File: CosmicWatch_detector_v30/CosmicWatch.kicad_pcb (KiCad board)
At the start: 2 copper layers, 140.8 x 104 mm, 115 parts, among them J3 RJ45, P1 CONN_01X04, P10 CONN_02X02, P11 CONN_01X01, P12 CONN_01X01, P13 CONN_01X01, P14 CONN_01X01, P15 CONN_02X04, P16 CONN_01X02, P19 CONN_01X01, P2 CONN_01X01, P29 CONN_01X01, P3 CONN_01X04, P30 CONN_01X01, P32 CONN_01X04, P4 CONN_01X04, P5 CONN_01X02, P7 CONN_01X01, P8 CONN_01X01, SW1 RESET, U1 MAX5026, U10 SiPM_AFBR-S4N33C013, U12 LTC6752, U13 TS5A1066, U16 UMCC, U17 UMCC, U19 LMH6658, U2 SiPM_MicroFJ−300XX−TSV, U22 UMCC, U23 UMCC, U3 MMCX, U4 TS5A1066, U5 RasberryPi_Pico, U6 LMH6658, U7 TPS6040X, U8 sd_card_socket, U9 2NPNMBT6429DW1T1G

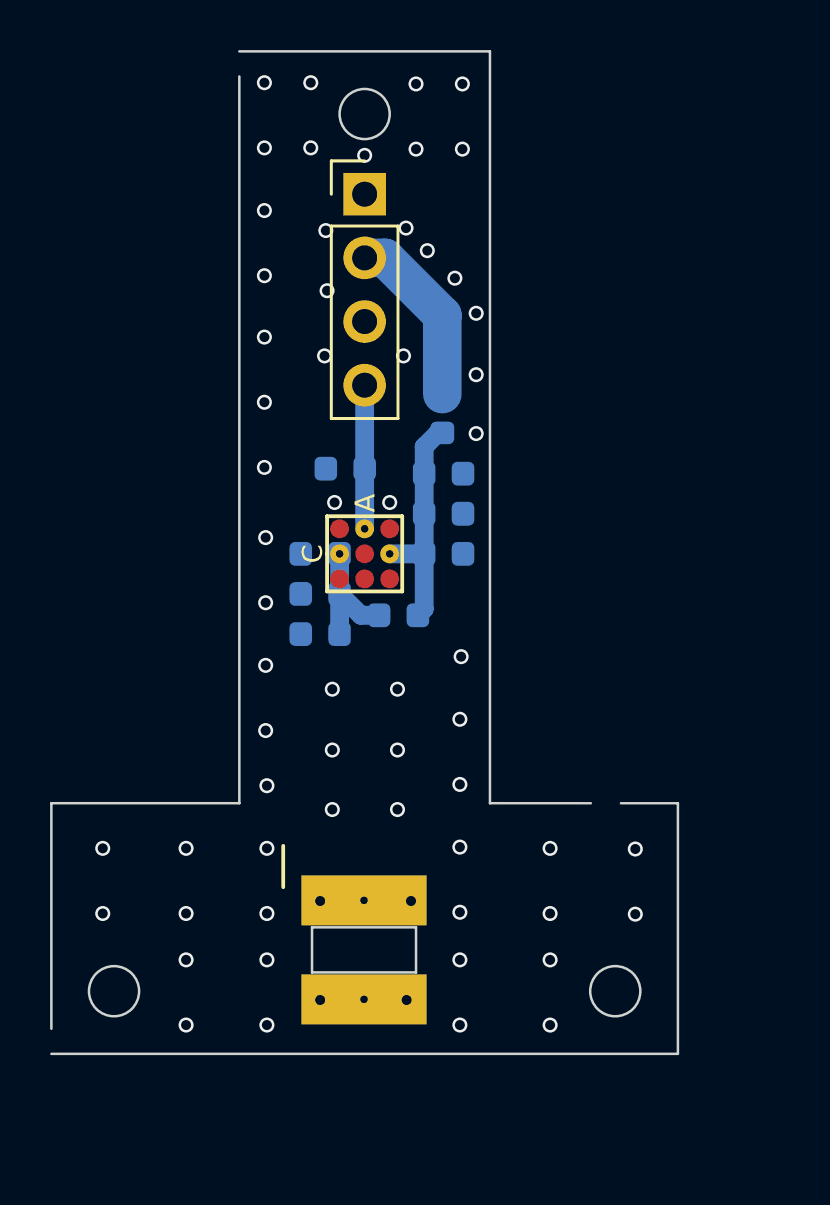
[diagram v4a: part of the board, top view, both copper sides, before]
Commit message: removing second sipm
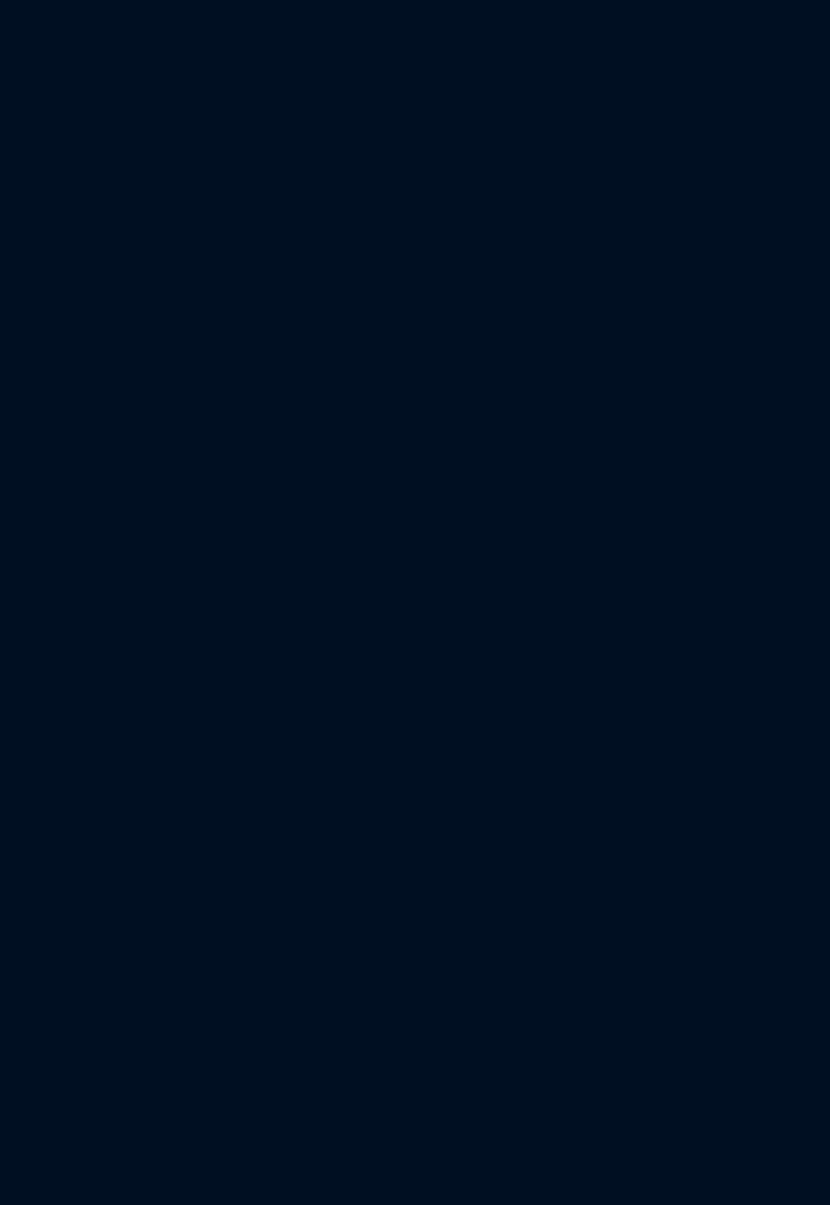
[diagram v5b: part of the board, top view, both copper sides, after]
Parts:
- removed C29, C34: 100n, Capacitor_SMD:C_0603_1608Metric
- removed C30, C33: 10nF, Capacitor_SMD:C_0603_1608Metric
- removed C31, C32: 10p, Capacitor_SMD:C_0603_1608Metric
- removed P29, P30: CONN_01X01, Connector_PinHeader_2.54mm:PinHeader_1x01_P2.54mm_Vertical
- removed P32: CONN_01X04, Connector_PinHeader_2.54mm:PinHeader_1x04_P2.54mm_Vertical
- removed R22, R34, R35: 10, Capacitor_SMD:C_0603_1608Metric
- removed U10: SiPM_AFBR-S4N33C013, MyFootprints:SiPM_S4N33C013
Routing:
- net Net-(U10-c2): track 9.16 -> 0.00 mm
- net Net-(P32-P2): track 7.19 -> 0.00 mm
- net Net-(P32-P4): track 5.73 -> 0.00 mm
- net Net-(U10-c1): track 5.13 -> 0.00 mm
- net unconnected-(P30-P1-Pad1): vias 2 -> 0
- net unconnected-(P29-P1-Pad1): vias 2 -> 0
- net GNDA: vias 298 -> 238
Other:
- board size 140.8 x 104 mm -> 99.9 x 99.9 mm
- board text removed: "AFBR-S4N33C013"

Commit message: updating netlist and deleting unnecessary components from PCB
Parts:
- removed C21, C35, C45: 0.1uF, Capacitor_SMD:C_0603_1608Metric
- removed C23, C43, C44, C5: 10nF, Capacitor_SMD:C_0603_1608Metric
- removed C36, C46: 2nF, Capacitor_SMD:C_0603_1608Metric
- removed C38: 2.2uF, Capacitor_SMD:C_0603_1608Metric
- removed C48: 1nF, Capacitor_SMD:C_0603_1608Metric
- removed R15, R16: 200, Capacitor_SMD:C_0603_1608Metric
- removed R18, R24, R40, R42: 100k, Capacitor_SMD:C_0603_1608Metric
- removed R19, R21, R31: 10k, Capacitor_SMD:C_0603_1608Metric
- removed R23: 20, Capacitor_SMD:C_0603_1608Metric
- removed R28: 100, Capacitor_SMD:C_0603_1608Metric
- removed R5: 1k, Capacitor_SMD:C_0603_1608Metric
- removed U12: LTC6752, Package_TO_SOT_SMD:SOT-23-6
- removed U19: LMH6658, Package_SO:SOIC-8_3.9x4.9mm_P1.27mm
- removed U22, U23: UMCC, MyFootprints:UMCC
- removed U4: TS5A1066, Package_TO_SOT_SMD:SOT-23-5
- added C10: 10n, Capacitor_SMD:C_0603_1608Metric, F.Cu at (118.2, 82.4)
- added C11: 2nF, Capacitor_SMD:C_0603_1608Metric, F.Cu at (118.2, 84.9)
- added C12: 0.1uF, Capacitor_SMD:C_0603_1608Metric, F.Cu at (118.2, 87.4)
- added C13: 10nF, Capacitor_SMD:C_0603_1608Metric, F.Cu at (118.2, 89.9)
- added C18: 10nF, Capacitor_SMD:C_0603_1608Metric, F.Cu at (118.2, 92.4)
- added C9: 10nF, Capacitor_SMD:C_0603_1608Metric, F.Cu at (118.2, 79.9)
- added Q1: 2N7002, Package_TO_SOT_SMD:SOT-23, F.Cu at (122.7, 80.8)
- C19: value 0.1uF -> 10n
- C6: value 10nF -> 0.1uF
- C8: value 10n -> 10nF
- D2, D3: value DIODE -> D_Schottky; footprint Diode_SMD:D_SOD-123 -> Diode_SMD:D_SOD-523
- R1: value 200 -> 47k
- R11: value 47k -> 100
- R13: value 150 -> 10k
- R14: value 2k -> 100
- R4: value 200 -> 1k
- R6: value 49.9 -> 10k
- R9: value 1k -> 100
- U9: value 2NPNMBT6429DW1T1G -> LMH6658; footprint Package_TO_SOT_SMD:SOT-23-6 -> Package_SO:SOIC-8_3.9x4.9mm_P1.27mm
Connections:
- C19 pad 1: GNDA -> VCC
- C19 pad 2: VEE -> GNDA
- C6 pad 1: VCC -> GNDA
- C6 pad 2: GNDA -> VEE
- C8 pad 1: VCC -> GNDA
- C8 pad 2: GNDA -> VEE
- D2 pad 1: Net-(D2-A) -> Net-(D2-K)
- D2 pad 2: Net-(D2-K) -> Net-(D2-A)
- D3 pad 1: SNG2 -> Net-(D3-K)
- D3 pad 2: Net-(D2-A) -> Net-(D2-K)
- R1 pad 1: Net-(C46-Pad1) -> SiPM
- R1 pad 2: SNG2 -> GNDA
- R11 pad 1: SiPM -> SNG1
- R11 pad 2: GNDA -> Net-(D2-K)
- R12 pad 1: AMP1 -> GNDA
- R12 pad 2: Net-(U19--INA) -> Net-(Q1-D)
- R13 pad 1: Net-(U6--INA) -> VCC
- R13 pad 2: GNDA -> Net-(U9--INB)
- R14 pad 1: AMP2 -> GNDA
- R14 pad 2: Net-(U6--INA) -> Net-(U9--INB)
- R3 pad 2: Net-(U19-+INA) -> Net-(U6-+INA)
- R4 pad 1: Net-(D2-A) -> Net-(U6--INA)
- R4 pad 2: Net-(U6-OUTB) -> GNDA
- R6 pad 2: Net-(U6-+INA) -> Net-(U6--INA)
- R9 pad 1: Net-(U19--INA) -> Net-(Q1-D)
- R9 pad 2: GNDA -> Net-(D3-K)
- U5 pad 31: SNG2 -> unconnected-(U5-ADC0-Pad31)
- U6 pad 1: AMP2 -> AMP1
- U6 pad 5: AMP2 -> AMP1
- U6 pad 6: Net-(D2-K) -> Net-(Q1-D)
- U6 pad 7: Net-(U6-OUTB) -> Net-(D2-A)
- U9 pad 1: Net-(U19--INB) -> SNG1
- U9 pad 2: Net-(R23-Pad1) -> SNG1
- U9 pad 3: Net-(R15-Pad2) -> Net-(Q1-D)
- U9 pad 4: SNG1 -> VEE
- U9 pad 5: Net-(R23-Pad1) -> AMP1
- U9 pad 6: Net-(R16-Pad1) -> Net-(U9--INB)
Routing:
- net SNG2: track 42.4 -> 0.00 mm, vias 3 -> 0
- net unconnected-(U5-ADC0-Pad31): track 0.00 -> 29.5 mm, vias 0 -> 1
- net (no net): track 0.00 -> 27.1 mm
- net AMP2: track 14.1 -> 0.00 mm
- net Net-(D2-A): track 13.3 -> 0.00 mm
- net Net-(R23-Pad1): track 9.65 -> 0.00 mm
- net Net-(D2-K): track 8.66 -> 0.00 mm, vias 0 -> 1
- net Net-(U19--INB): track 8.20 -> 0.00 mm
- net AMP1: track 34.3 -> 26.2 mm
- net Net-(Q1-D): track 0.00 -> 7.84 mm
- net Net-(U12--IN): track 4.81 -> 0.00 mm
- net Net-(U19--INA): track 4.23 -> 0.00 mm
- net Net-(U19-OUTB): track 2.69 -> 0.00 mm
- net Net-(U6-+INA): track 2.47 -> 4.67 mm
- net Net-(U19-+INA): track 2.20 -> 0.00 mm
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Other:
- board text removed: "TP3"
- board text removed: "TP4"

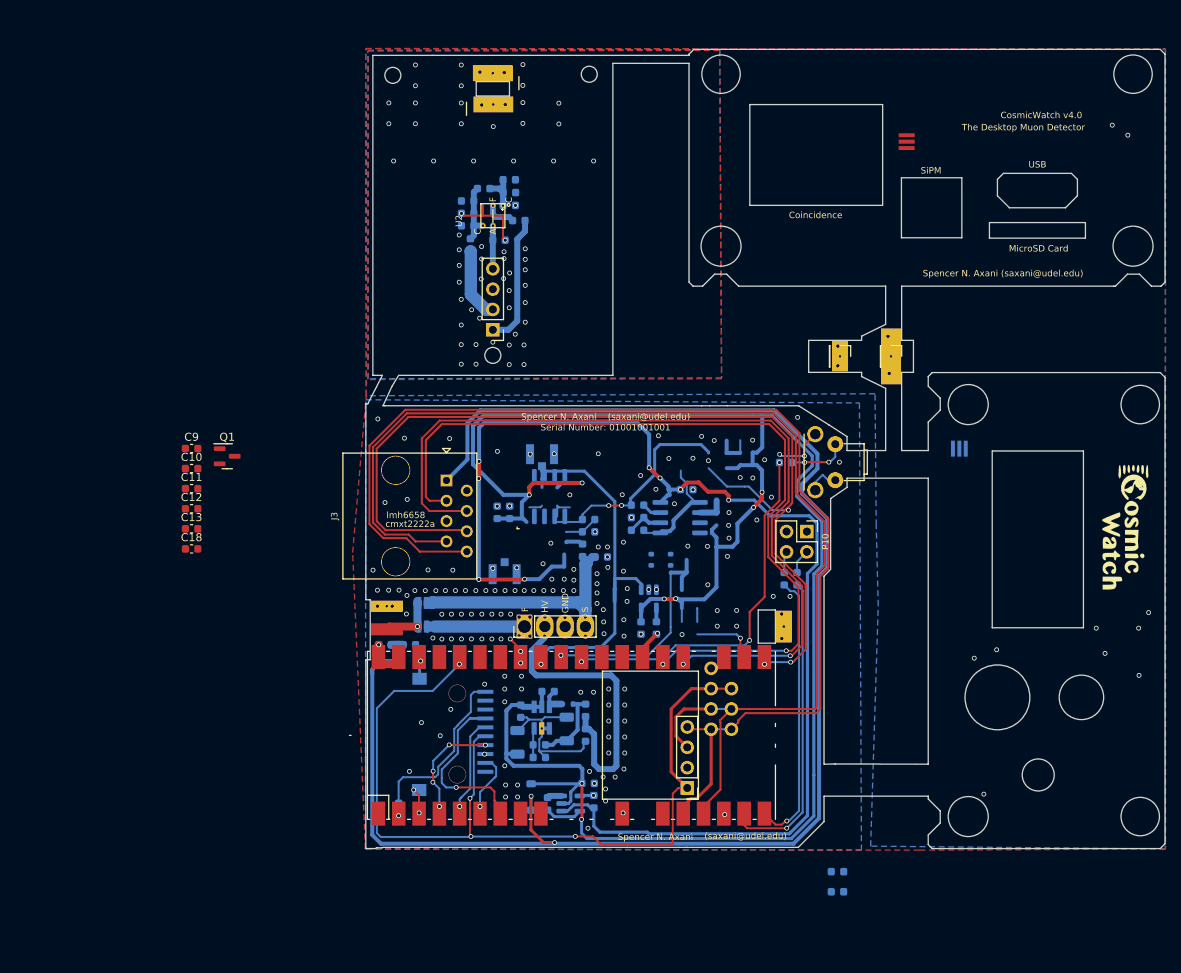
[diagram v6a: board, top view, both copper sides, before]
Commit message: rearranging peak detector in pcb
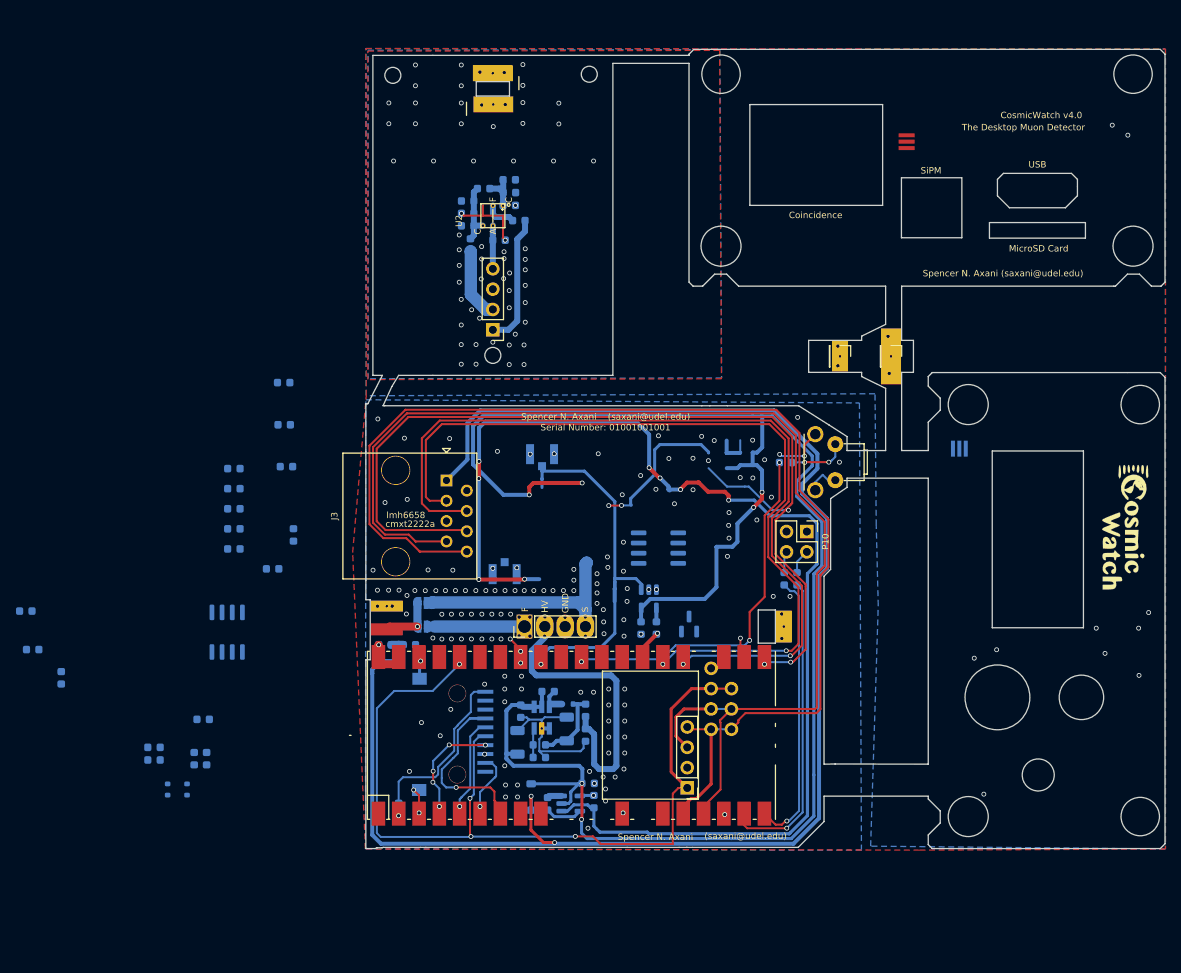
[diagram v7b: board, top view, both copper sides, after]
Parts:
- C10, C11, C12, C13, C18, C9, Q1: moved to B.Cu
- moved R4 107.4 mm to (97.5, 100.2)
- moved R1 104.4 mm to (98.3, 105.0)
- moved R3 67.1 mm to (101.9, 108.5)
- moved C19 66.9 mm to (119.6, 113.7)
- moved D2 66.9 mm to (115.2, 122.5)
- moved D3 66.9 mm to (117.6, 122.5)
- moved R13 66.9 mm to (113.5, 117.2)
- moved R14 66.9 mm to (113.5, 118.8)
- moved Q1 61.4 mm to (180.4, 101.8), turned to 90 degrees
- moved C6 48.8 mm to (120.1, 118.6)
- moved C8 48.8 mm to (118.5, 118.6)
- moved R6 44.1 mm to (130.1, 82.1)
- moved U9 43.7 mm to (122.6, 102.8)
- moved R12 41.8 mm to (129.7, 71.6)
- moved R11 41.1 mm to (128.3, 94.9)
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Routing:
- net unconnected-(U5-ADC0-Pad31): track 29.5 -> 1.13 mm, vias 1 -> 0
- net (no net): track 27.1 -> 4.81 mm
- net VCC: track 242.9 -> 229.0 mm, vias 9 -> 7
- net Net-(Q1-D): track 7.84 -> 0.00 mm
- net AMP1: track 26.2 -> 18.6 mm
- net VEE: track 157.8 -> 150.4 mm, vias 11 -> 8
- net TriggerReset2: track 8.39 -> 2.80 mm
- net Net-(U6-+INA): track 4.67 -> 0.00 mm
- net Net-(U6--INA): track 4.56 -> 0.00 mm
- net SiPM: track 30.6 -> 28.2 mm
- net Net-(U9--INB): vias 1 -> 0
- net Net-(D3-K): vias 1 -> 0
- net GNDA: vias 232 -> 218

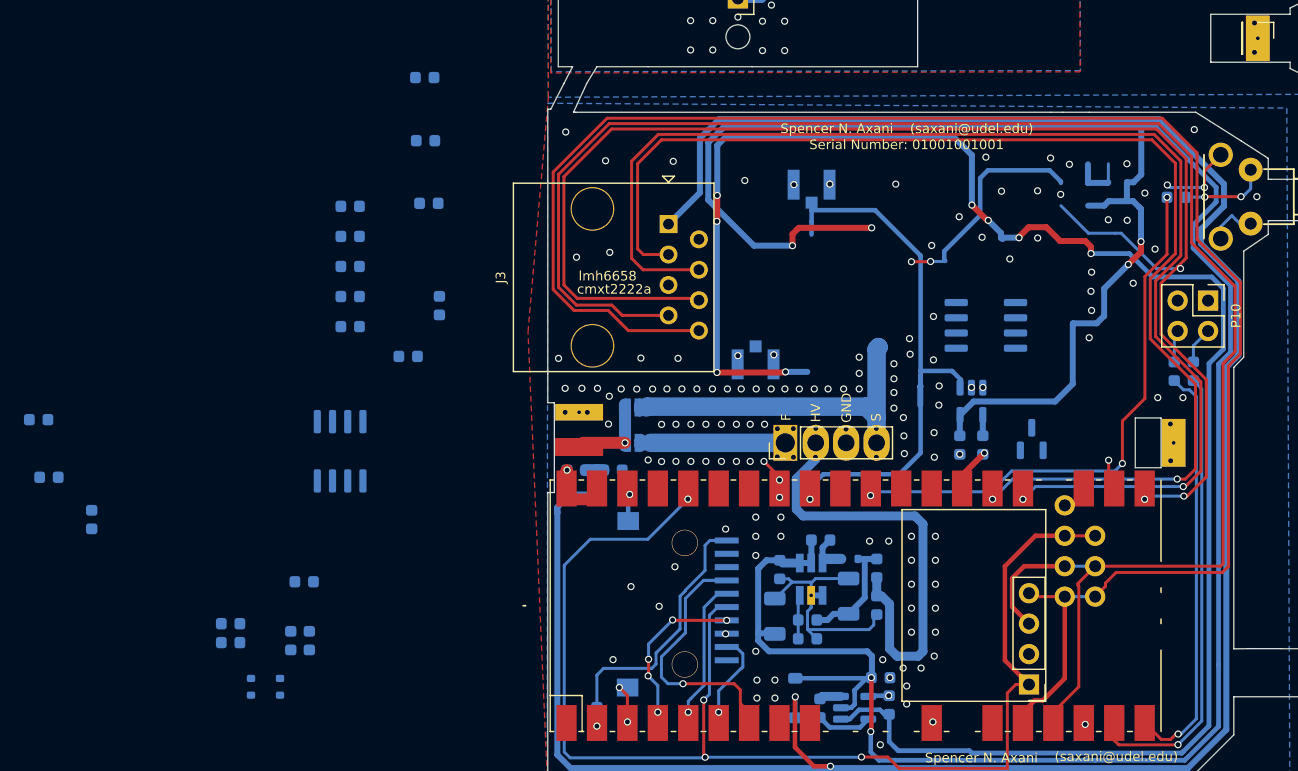
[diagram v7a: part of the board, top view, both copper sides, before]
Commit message: placing peak detector
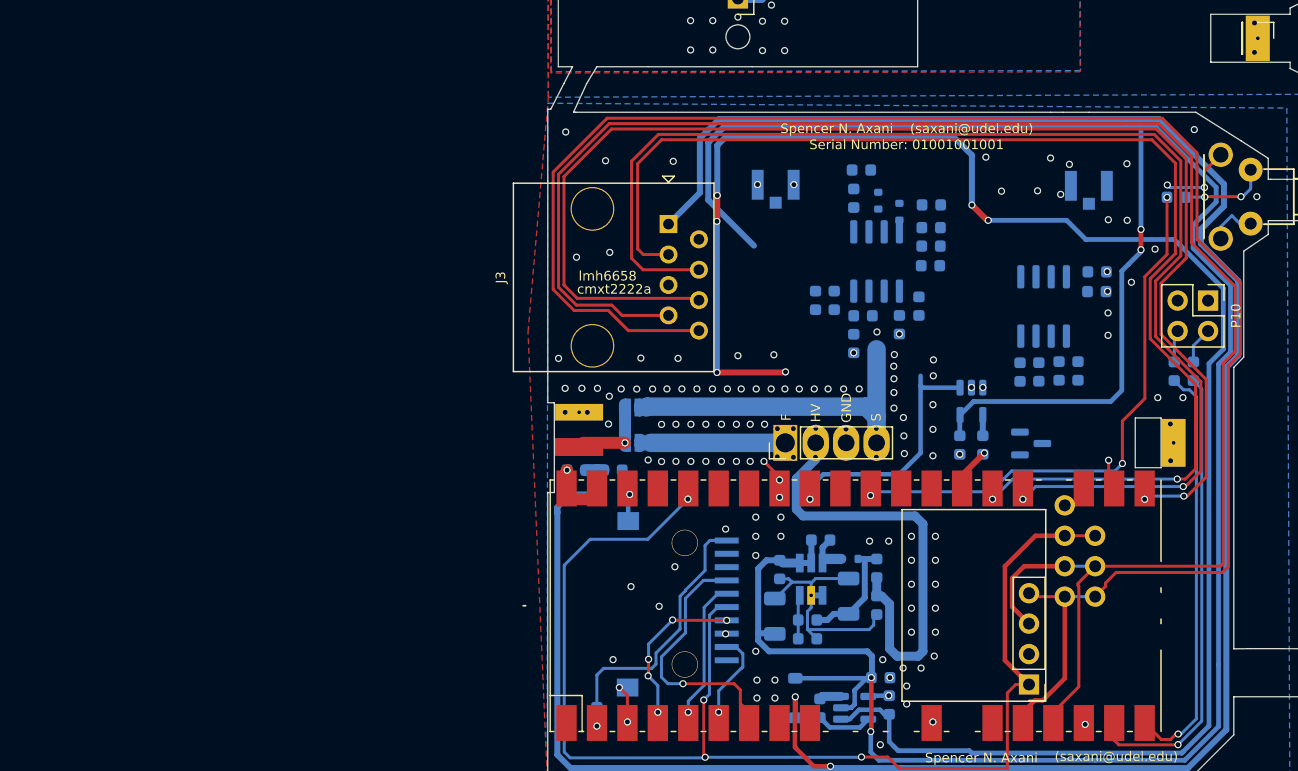
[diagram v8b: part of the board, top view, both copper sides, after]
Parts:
- moved R14 74.3 mm to (184.2, 96.1), turned to 90 degrees
- moved R13 72.3 mm to (182.7, 96.1), turned to 90 degrees
- moved R4 72.3 mm to (169.3, 92.2), turned to -90 degrees
- moved R1 68.1 mm to (165.5, 93.8), turned to -90 degrees
- moved R3 66.6 mm to (166.3, 91.5), turned to 0 degrees
- moved D2 66.3 mm to (167.6, 81.9)
- moved D3 65.2 mm to (169.3, 82.8), turned to -90 degrees
- moved C12 62.4 mm to (185.8, 87.8)
- moved C13 62.3 mm to (185.8, 89.5)
- moved C19 62.3 mm to (179.4, 96.2), turned to -90 degrees
- moved U9 60.0 mm to (181.4, 90.7), turned to -90 degrees
- moved C18 57.6 mm to (181.0, 96.2), turned to -90 degrees
- moved C6 52.2 mm to (163.9, 90.2)
- moved C8 52.2 mm to (162.3, 90.2)
- moved C10 48.5 mm to (172.0, 84.1)
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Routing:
- net SNG1: track 48.0 -> 21.2 mm, vias 1 -> 2
- net AMP1: track 18.6 -> 0.00 mm, vias 2 -> 0
- net VCC: track 229.0 -> 214.6 mm, vias 7 -> 4
- net TRG: track 122.8 -> 110.4 mm, vias 3 -> 2
- net (no net): track 4.81 -> 0.00 mm
- net VEE: track 150.4 -> 147.0 mm, vias 8 -> 6
- net Net-(D2-K): vias 1 -> 0
- net GNDA: vias 218 -> 210
